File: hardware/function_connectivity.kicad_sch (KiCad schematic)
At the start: 5 parts, among them J10 Conn_01x05_Pin, J8 USB_C_Receptacle_USB2.0, J9 Conn_01x05_Pin

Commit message: auto updated
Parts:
- renumbered J8 to J7, J9 to J8, J10 to J9, R3 to R24, R4 to R25
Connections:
- net USART_CK: now also J9.4 (Pin_4); no longer J9.3 (Pin_3)
- net USART_RX: now also J9.3 (Pin_3); no longer J9.2 (Pin_2)
- net USART_TX: now also J9.2 (Pin_2); no longer J9.4 (Pin_4)
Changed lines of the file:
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@@
 		)
 	)
-	(hierarchical_label "USART_CK"
+	(hierarchical_label "I2S_CK"
 		(shape bidirectional)
-		(at 222.25 127 180)
+		(at 222.25 60.96 180)
 		(fields_autoplaced yes)
 		(effects
@@
 		)
 	)
-	(hierarchical_label "I2S_CK"
-		(shape bidirectional)
-		(at 222.25 60.96 180)
+	(hierarchical_label "UCPD1_CC1"
+		(shape output)
+		(at 63.5 46.99 180)
 		(fields_autoplaced yes)
 		(effects
@@
 		)
 	)
-	(hierarchical_label "UCPD1_CC1"
+	(hierarchical_label "UCPD1_CC2"
 		(shape output)
-		(at 63.5 46.99 180)
+		(at 63.5 49.53 180)
 		(fields_autoplaced yes)
 		(effects
@@
 		)
 	)
-	(hierarchical_label "USART_RX"
+	(hierarchical_label "USB_D+"
 		(shape bidirectional)
-		(at 222.25 124.46 180)
+		(at 101.6 59.69 180)
 		(fields_autoplaced yes)
 		(effects
@@
 		)
 	)
-	(hierarchical_label "UCPD1_CC2"
-		(shape output)
-		(at 63.5 49.53 180)
+	(hierarchical_label "I2S_WS"
+		(shape bidirectional)
+		(at 222.25 63.5 180)
 		(fields_autoplaced yes)
 		(effects
@@
 		)
 	)
-	(hierarchical_label "USB_D+"
+	(hierarchical_label "USB_D-"
 		(shape bidirectional)
-		(at 101.6 59.69 180)
+		(at 101.6 54.61 180)
 		(fields_autoplaced yes)
 		(effects
@@
 		)
 	)
-	(hierarchical_label "I2S_WS"
+	(hierarchical_label "USART_TX"
 		(shape bidirectional)
-		(at 222.25 63.5 180)
+		(at 222.25 124.46 180)
 		(fields_autoplaced yes)
 		(effects
@@
 		)
 	)
-	(hierarchical_label "USB_D-"
+	(hierarchical_label "USART_RX"
 		(shape bidirectional)
-		(at 101.6 54.61 180)
+		(at 222.25 127 180)
 		(fields_autoplaced yes)
 		(effects
@@
 		)
 	)
-	(hierarchical_label "USART_TX"
+	(hierarchical_label "USART_CK"
 		(shape bidirectional)
 		(at 222.25 129.54 180)
@@
 		(dnp no)
 		(fields_autoplaced yes)
-		(property "Reference" "#PWR026"
+		(property "Reference" "#PWR054"
 			(at 69.85 70.485 0)
 			(effects
@@
 			(project "function_gen"
 				(path "/612821d8-1ef1-4cb8-a651-a5a0edc165c6/d9c2c47e-bc23-42cd-8857-93f813dbd6d6"
-					(reference "#PWR026")
+					(reference "#PWR054")
 					(unit 1)
 				)
@@
 		(dnp no)
 		(fields_autoplaced yes)
-		(property "Reference" "#PWR035"
+		(property "Reference" "#PWR061"
 			(at 222.25 144.78 0)
 			(effects
@@
 			(project "function_gen"
 				(path "/612821d8-1ef1-4cb8-a651-a5a0edc165c6/d9c2c47e-bc23-42cd-8857-93f813dbd6d6"
-					(reference "#PWR035")
+					(reference "#PWR061")
 					(unit 1)
 				)
@@
 		(on_board yes)
 		(dnp no)
-		(property "Reference" "J10"
+		(property "Reference" "J9"
 			(at 233.045 116.84 0)
 			(effects
@@
 			(project "function_gen"
 				(path "/612821d8-1ef1-4cb8-a651-a5a0edc165c6/d9c2c47e-bc23-42cd-8857-93f813dbd6d6"
-					(reference "J10")
+					(reference "J9")
 					(unit 1)
 				)
@@
 		(dnp no)
 		(fields_autoplaced yes)
-		(property "Reference" "#PWR032"
+		(property "Reference" "#PWR058"
 			(at 222.25 55.88 0)
 			(effects
@@
 			(project "function_gen"
 				(path "/612821d8-1ef1-4cb8-a651-a5a0edc165c6/d9c2c47e-bc23-42cd-8857-93f813dbd6d6"
-					(reference "#PWR032")
+					(reference "#PWR058")
 					(unit 1)
 				)
@@
 		(dnp no)
 		(fields_autoplaced yes)
-		(property "Reference" "#PWR030"
+		(property "Reference" "#PWR056"
 			(at 109.22 43.18 0)
 			(effects
@@
 			(project "function_gen"
 				(path "/612821d8-1ef1-4cb8-a651-a5a0edc165c6/d9c2c47e-bc23-42cd-8857-93f813dbd6d6"
-					(reference "#PWR030")
+					(reference "#PWR056")
 					(unit 1)
 				)
@@
 		(dnp no)
 		(fields_autoplaced yes)
-		(property "Reference" "#PWR031"
+		(property "Reference" "#PWR057"
 			(at 127 88.9 0)
 			(effects
@@
 			(project "function_gen"
 				(path "/612821d8-1ef1-4cb8-a651-a5a0edc165c6/d9c2c47e-bc23-42cd-8857-93f813dbd6d6"
-					(reference "#PWR031")
+					(reference "#PWR057")
 					(unit 1)
 				)
@@
 		(dnp yes)
 		(fields_autoplaced yes)
-		(property "Reference" "R4"
+		(property "Reference" "R25"
 			(at 85.09 57.785 0)
 			(effects
@@
 			(project "function_gen"
 				(path "/612821d8-1ef1-4cb8-a651-a5a0edc165c6/d9c2c47e-bc23-42cd-8857-93f813dbd6d6"
-					(reference "R4")
+					(reference "R25")
 					(unit 1)
 				)
@@
 		(dnp no)
 		(fields_autoplaced yes)
-		(property "Reference" "#PWR027"
+		(property "Reference" "#PWR055"
 			(at 82.55 70.485 0)
 			(effects
@@
 			(project "function_gen"
 				(path "/612821d8-1ef1-4cb8-a651-a5a0edc165c6/d9c2c47e-bc23-42cd-8857-93f813dbd6d6"
-					(reference "#PWR027")
+					(reference "#PWR055")
 					(unit 1)
 				)
@@
 		(on_board yes)
 		(dnp no)
-		(property "Reference" "J9"
+		(property "Reference" "J8"
 			(at 233.045 50.8 0)
 			(effects
@@
 			(project "function_gen"
 				(path "/612821d8-1ef1-4cb8-a651-a5a0edc165c6/d9c2c47e-bc23-42cd-8857-93f813dbd6d6"
-					(reference "J9")
+					(reference "J8")
 					(unit 1)
 				)
@@
 		(on_board yes)
 		(dnp no)
-		(property "Reference" "J8"
+		(property "Reference" "J7"
 			(at 127 34.925 0)
 			(effects
@@
 			(project "function_gen"
 				(path "/612821d8-1ef1-4cb8-a651-a5a0edc165c6/d9c2c47e-bc23-42cd-8857-93f813dbd6d6"
-					(reference "J8")
+					(reference "J7")
 					(unit 1)
 				)
@@
 		(dnp no)
 		(fields_autoplaced yes)
-		(property "Reference" "#PWR034"
+		(property "Reference" "#PWR060"
 			(at 222.25 119.38 0)
 			(effects
@@
 			(project "function_gen"
 				(path "/612821d8-1ef1-4cb8-a651-a5a0edc165c6/d9c2c47e-bc23-42cd-8857-93f813dbd6d6"
-					(reference "#PWR034")
+					(reference "#PWR060")
 					(unit 1)
 				)
@@
 		(dnp no)
 		(fields_autoplaced yes)
-		(property "Reference" "#PWR033"
+		(property "Reference" "#PWR059"
 			(at 222.25 77.47 0)
 			(effects
@@
 			(project "function_gen"
 				(path "/612821d8-1ef1-4cb8-a651-a5a0edc165c6/d9c2c47e-bc23-42cd-8857-93f813dbd6d6"
-					(reference "#PWR033")
+					(reference "#PWR059")
 					(unit 1)
 				)
@@
 		(dnp yes)
 		(fields_autoplaced yes)
-		(property "Reference" "R3"
+		(property "Reference" "R24"
 			(at 72.39 57.785 0)
 			(effects
@@
 			(project "function_gen"
 				(path "/612821d8-1ef1-4cb8-a651-a5a0edc165c6/d9c2c47e-bc23-42cd-8857-93f813dbd6d6"
-					(reference "R3")
-					(unit 1)
-				)
+					(reference "R24")
+					(unit 1)
+				)

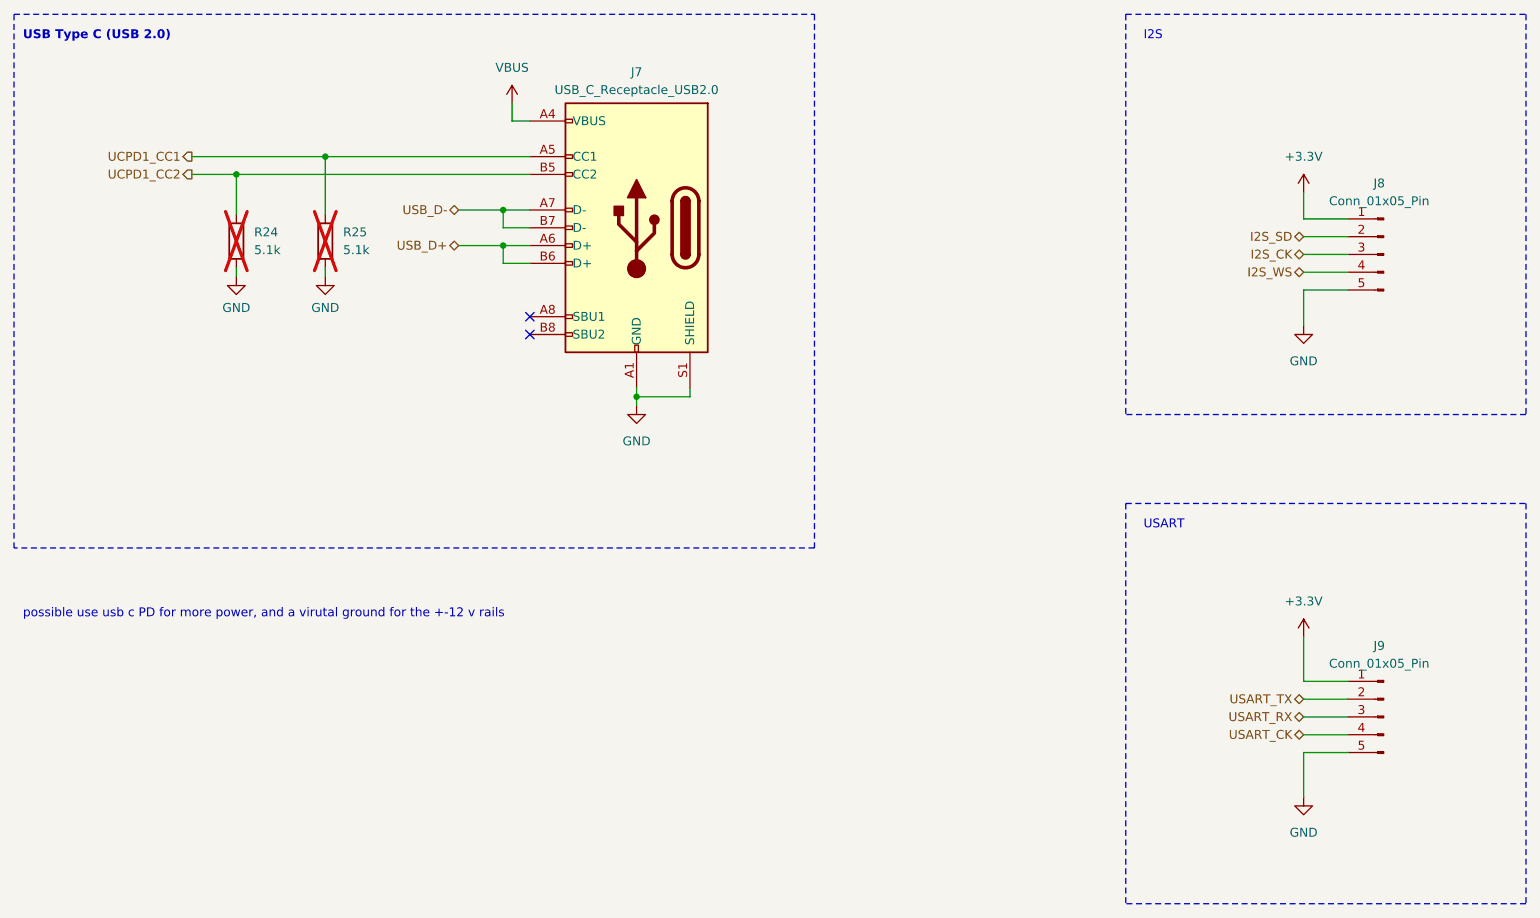
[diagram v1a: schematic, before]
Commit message: added tvs diodes for eds
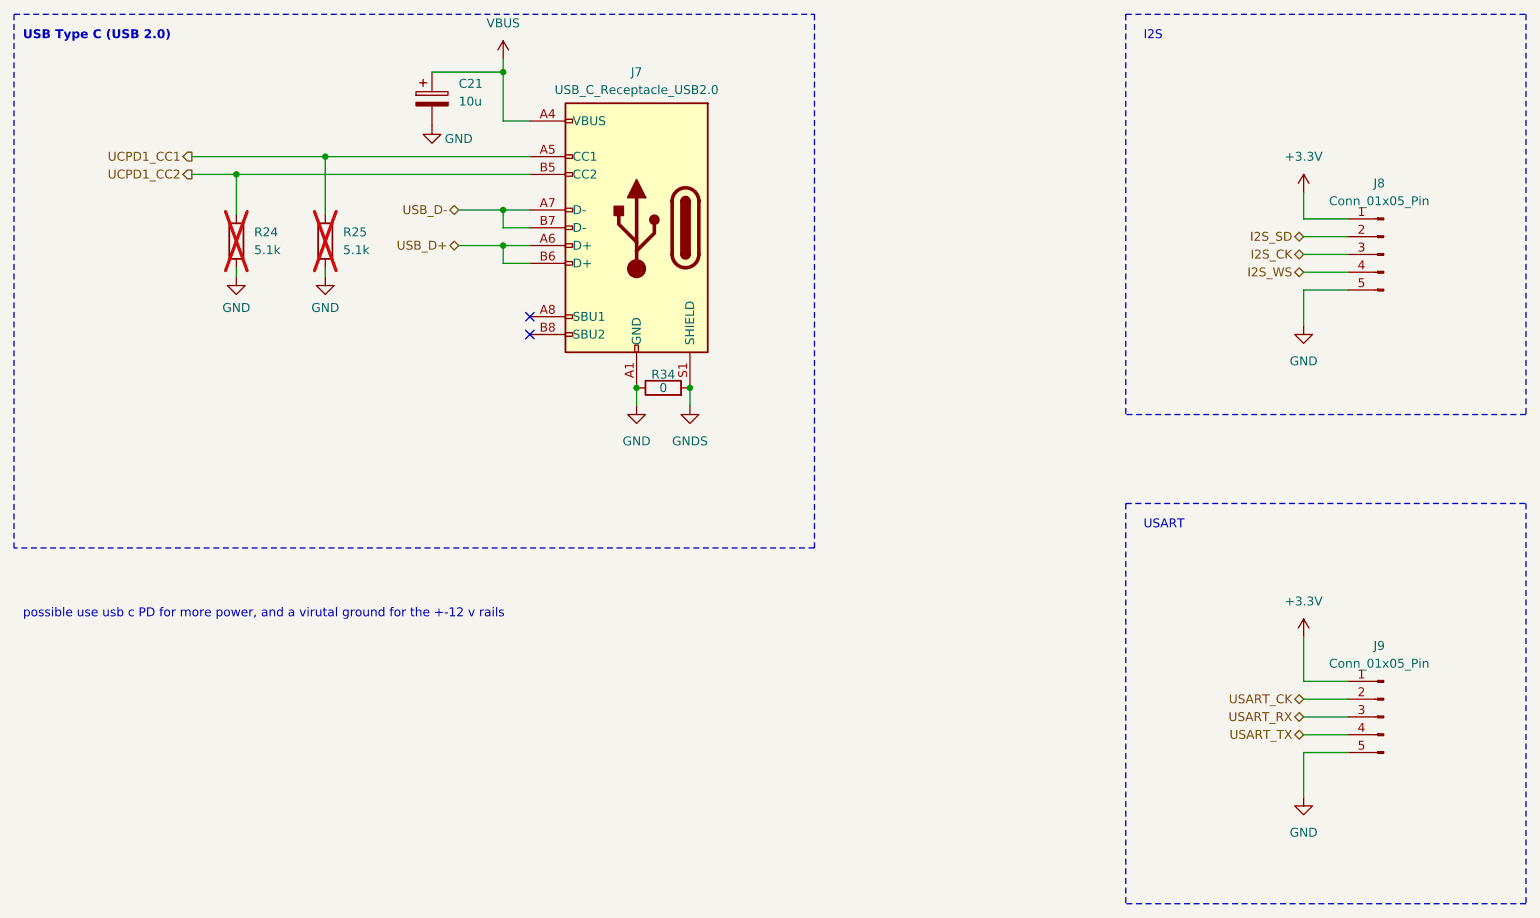
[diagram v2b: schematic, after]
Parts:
- added C21: 10u, Capacitor_SMD:C_0805_2012Metric, symbol Device:C_Polarized
- added R34: 0, Resistor_SMD:R_0805_2012Metric, symbol Device:R
- J8, J9: footprint Connector_PinHeader_2.54mm:PinHeader_1x05_P2.54mm_Vertical -> Connector_JST:JST_XH_B5B-XH-AM_1x05_P2.50mm_Vertical
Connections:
- net GND: now also C21.2, R34.1; no longer J7.S1 (SHIELD)
- net USART_CK: now also J9.2 (Pin_2); no longer J9.4 (Pin_4)
- net USART_TX: now also J9.4 (Pin_4); no longer J9.2 (Pin_2)
- net VBUS: now also C21.1
- new net GNDS: J7.S1 (SHIELD), R34.2

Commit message: updated
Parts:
- removed R34: 0, Resistor_SMD:R_0805_2012Metric, symbol Device:R
- added D19, D20, D21: SP0504BAHT, Package_TO_SOT_SMD:SOT-23-5, symbol Power_Protection:SP0504BAHT
- added D26: PTVS5V0Z1USK, Diode_SMD:Nexperia_DSN1608-2_1.6x0.8mm, symbol Diode:PTVS5V0Z1USK
- added D27: D_Schottky, Diode_SMD:D_0805_2012Metric, symbol Device:D_Schottky
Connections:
- net GNDS is gone; now on net GND: J7.S1 (SHIELD)
- net +3.3V: now also D20.1 (K), D21.1 (K)
- net GND: now also D19.2 (A), D20.2 (A), D21.2 (A), D26.2 (A)
- net I2S_CK: now also D20.4 (K)
- net I2S_SD: now also D20.3 (K)
- net I2S_WS: now also D20.5 (K)
- net UCPD1_CC1: now also D19.1 (K)
- net UCPD1_CC2: now also D19.3 (K)
- net USART_CK: now also D21.3 (K)
- net USART_RX: now also D21.4 (K)
- net USART_TX: now also D21.5 (K)
- net USB_D+: now also D19.4 (K)
- net USB_D-: now also D19.5 (K)
- net VBUS: now also D27.1 (K); no longer C21.1, J7.A4 (VBUS), J7.A9 (VBUS), J7.B4 (VBUS), J7.B9 (VBUS)
- new net: C21.1, D26.1 (K), D27.2 (A), J7.A4 (VBUS), J7.A9 (VBUS), J7.B4 (VBUS), J7.B9 (VBUS)
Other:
- moved on the sheet: C21, J9, R24, R25
